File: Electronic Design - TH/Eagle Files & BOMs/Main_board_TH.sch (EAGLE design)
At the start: 41 parts, among them M1 ARDUINO-NANO-3.0, Q1 IRF9520, Q2 IRF9520

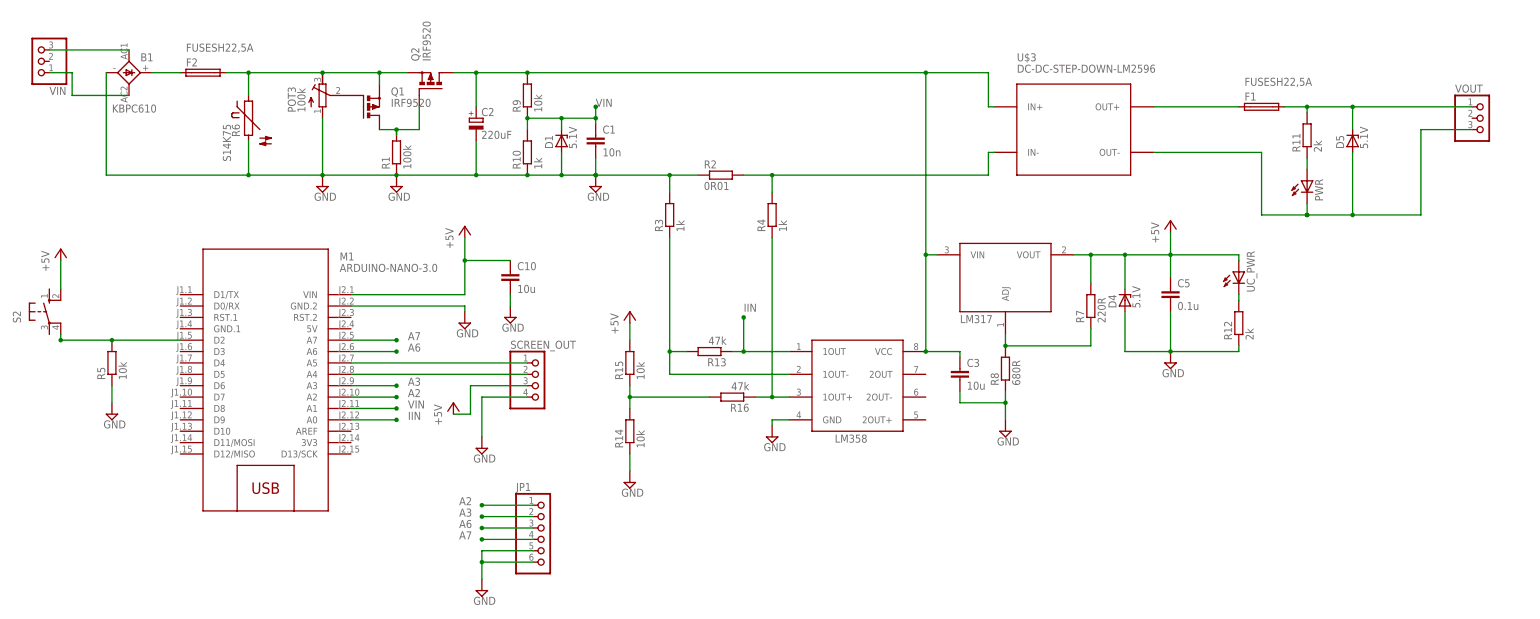
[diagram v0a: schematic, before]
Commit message: Removed: pin headers for arduino, button for arduino and LED for LM2596. Inital board layout complete. Sub modules pretty much done but overall layout still needs work
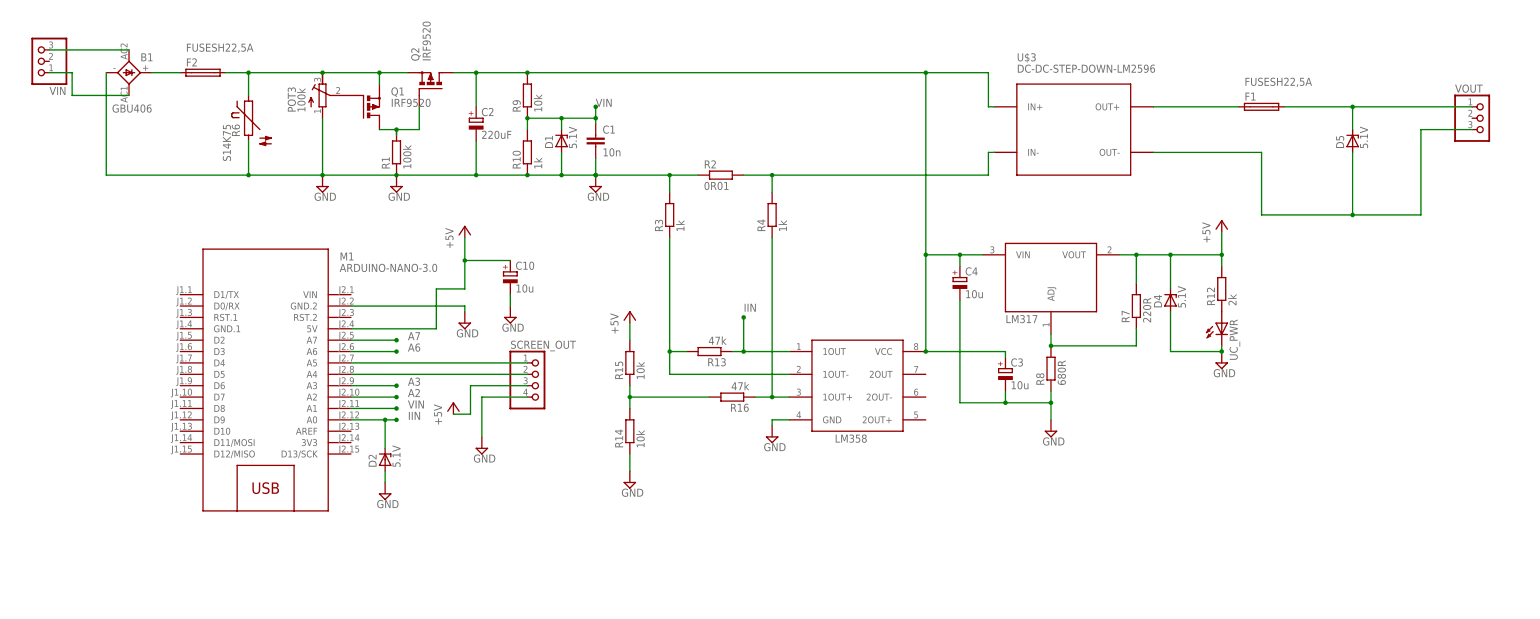
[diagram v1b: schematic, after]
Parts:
- removed C5: 0.1u, resistor:C-EU050-024X044
- removed JP1: (no value), pinhead:PINHD-1X6
- removed PWR: (no value), led:LED3MM
- removed R11: 2k, resistor:R-EU_0207/10
- removed R5: 10k, resistor:R-EU_0207/10
- removed S2: (no value), switch-omron:10-XX
- removed U$1: LM317, Samson:LM317
- added C4: 10u, resistor:CPOL-EUE2.5-7
- added D2: 5.1V, diode:ZPD
- added LM317: LM317, Samson:LM317
- B1: value KBPC610 -> GBU406; device rectifier:GBPC6 -> rectifier:GBU4
- C10, C3: device resistor:C-EU050-024X044 -> resistor:CPOL-EUE2.5-7
- Q1, Q2: device Samson:PMOSFET_PTO220BH -> Samson:PMOSFET_PTO220BV
- renumbered U$2 to LM358
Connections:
- net N$2 renamed A4
- net N$3 renamed A5
- removed net BUTTON: M1.D2, R5.2, S2.P1
- removed net N$18: PWR.A, R11.1
- removed net N$28: R12.2, UC_PWR.C
- new net N$2: R12.1, UC_PWR.A
- net +5V: now also C10.+, LM317.VOUT, M1.5V, R12.2; no longer C10.1, C5.1, M1.VIN, S2.S1, U$1.VOUT, UC_PWR.A
- net A2: no longer JP1.1
- net A3: no longer JP1.2
- net A6: no longer JP1.3
- net A7: no longer JP1.4
- net GND: now also C10.-, C3.-, C4.-, D2.A, UC_PWR.C; no longer C10.2, C3.2, C5.2, JP1.5, JP1.6, R12.1, R5.1
- net IIN: now also D2.C
- net N$10: no longer PWR.C
- net N$23: now also LM317.ADJ; no longer U$1.ADJ
- net VIN_PROTECTED: now also C3.+, C4.+, LM317.VIN; no longer C3.1, U$1.VIN
- net VOUT_FINAL: no longer R11.2
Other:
- moved on the sheet: D4, R12, R7, R8, UC_PWR

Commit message: high level layout complete and adding in BOM
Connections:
- removed net A6: M1.A6
- removed net A7: M1.A7
- removed net IIN: D2.C, LM358.1OUT, M1.A0, R13.1
- removed net VIN: C1.1, D1.C, M1.A1, R10.2, R9.1
- new net A0: D2.C, M1.A0
- new net A1: M1.A1
- new net I_IN: LM358.1OUT, M1.A6, R13.1
- new net V_IN: C1.1, D1.C, M1.A7, R10.2, R9.1
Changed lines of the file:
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@@
 </busses>
 <nets>
-<net name="VIN" class="0">
-<segment>
-<wire x1="-5.08" y1="77.47" x2="-5.08" y2="78.74" width="0.1524" layer="91"/>
-<junction x="-5.08" y="81.28"/>
-<label x="-5.08" y="81.28" size="1.778" layer="95"/>
-<pinref part="C1" gate="G$1" pin="1"/>
-<wire x1="-5.08" y1="78.74" x2="-5.08" y2="81.28" width="0.1524" layer="91"/>
-<wire x1="-12.7" y1="76.2" x2="-12.7" y2="78.74" width="0.1524" layer="91"/>
-<wire x1="-12.7" y1="78.74" x2="-5.08" y2="78.74" width="0.1524" layer="91"/>
-<junction x="-5.08" y="78.74"/>
-<pinref part="D1" gate="G$1" pin="C"/>
-<pinref part="R9" gate="G$1" pin="1"/>
-<wire x1="-12.7" y1="78.74" x2="-20.32" y2="78.74" width="0.1524" layer="91"/>
-<pinref part="R10" gate="G$1" pin="2"/>
-<wire x1="-20.32" y1="78.74" x2="-20.32" y2="76.2" width="0.1524" layer="91"/>
-<junction x="-20.32" y="78.74"/>
-<junction x="-12.7" y="78.74"/>
-</segment>
-<segment>
-<junction x="-49.53" y="13.97"/>
-<label x="-46.99" y="13.97" size="1.778" layer="95"/>
-<wire x1="-49.53" y1="13.97" x2="-59.69" y2="13.97" width="0.1524" layer="91"/>
-<pinref part="M1" gate="G$1" pin="A1"/>
-</segment>
-</net>
-<net name="IIN" class="0">
-<segment>
-<junction x="-49.53" y="11.43"/>
-<label x="-46.99" y="11.43" size="1.778" layer="95"/>
-<wire x1="-59.69" y1="11.43" x2="-52.07" y2="11.43" width="0.1524" layer="91"/>
-<pinref part="M1" gate="G$1" pin="A0"/>
-<pinref part="D2" gate="G$1" pin="C"/>
-<wire x1="-52.07" y1="11.43" x2="-49.53" y2="11.43" width="0.1524" layer="91"/>
-<wire x1="-52.07" y1="11.43" x2="-52.07" y2="5.08" width="0.1524" layer="91"/>
-<junction x="-52.07" y="11.43"/>
-</segment>
-<segment>
-<pinref part="R13" gate="G$1" pin="1"/>
-<pinref part="LM358" gate="G$1" pin="1OUT"/>
-<wire x1="25.4" y1="26.67" x2="27.94" y2="26.67" width="0.1524" layer="91"/>
-<wire x1="29.21" y1="26.67" x2="38.1" y2="26.67" width="0.1524" layer="91"/>
-<wire x1="29.21" y1="26.67" x2="27.94" y2="26.67" width="0.1524" layer="91"/>
-<wire x1="27.94" y1="26.67" x2="27.94" y2="34.29" width="0.1524" layer="91"/>
-<junction x="27.94" y="34.29"/>
-<label x="27.94" y="35.56" size="1.778" layer="95"/>
-<junction x="27.94" y="26.67"/>
-</segment>
-</net>
 <net name="GND" class="0">
 <segment>
@@
 </segment>
 </net>
-<net name="A6" class="0">
-<segment>
-<pinref part="M1" gate="G$1" pin="A6"/>
-<wire x1="-59.69" y1="26.67" x2="-49.53" y2="26.67" width="0.1524" layer="91"/>
-<junction x="-49.53" y="26.67"/>
-<label x="-46.99" y="26.67" size="1.778" layer="95"/>
-</segment>
-</net>
-<net name="A7" class="0">
-<segment>
-<pinref part="M1" gate="G$1" pin="A7"/>
-<wire x1="-59.69" y1="29.21" x2="-49.53" y2="29.21" width="0.1524" layer="91"/>
-<junction x="-49.53" y="29.21"/>
-<label x="-46.99" y="29.21" size="1.778" layer="95"/>
-</segment>
-</net>
 <net name="N$4" class="0">
 <segment>
@@
 </segment>
 </net>
+<net name="V_IN" class="0">
+<segment>
+<wire x1="-5.08" y1="77.47" x2="-5.08" y2="78.74" width="0.1524" layer="91"/>
+<junction x="-5.08" y="81.28"/>
+<label x="-5.08" y="81.28" size="1.778" layer="95"/>
+<pinref part="C1" gate="G$1" pin="1"/>
+<wire x1="-5.08" y1="78.74" x2="-5.08" y2="81.28" width="0.1524" layer="91"/>
+<wire x1="-12.7" y1="76.2" x2="-12.7" y2="78.74" width="0.1524" layer="91"/>
+<wire x1="-12.7" y1="78.74" x2="-5.08" y2="78.74" width="0.1524" layer="91"/>
+<junction x="-5.08" y="78.74"/>
+<pinref part="D1" gate="G$1" pin="C"/>
+<pinref part="R9" gate="G$1" pin="1"/>
+<wire x1="-12.7" y1="78.74" x2="-20.32" y2="78.74" width="0.1524" layer="91"/>
+<pinref part="R10" gate="G$1" pin="2"/>
+<wire x1="-20.32" y1="78.74" x2="-20.32" y2="76.2" width="0.1524" layer="91"/>
+<junction x="-20.32" y="78.74"/>
+<junction x="-12.7" y="78.74"/>
+</segment>
+<segment>
+<pinref part="M1" gate="G$1" pin="A7"/>
+<wire x1="-59.69" y1="29.21" x2="-49.53" y2="29.21" width="0.1524" layer="91"/>
+<junction x="-49.53" y="29.21"/>
+<label x="-46.99" y="29.21" size="1.778" layer="95"/>
+</segment>
+</net>
+<net name="I_IN" class="0">
+<segment>
+<pinref part="R13" gate="G$1" pin="1"/>
+<pinref part="LM358" gate="G$1" pin="1OUT"/>
+<wire x1="25.4" y1="26.67" x2="27.94" y2="26.67" width="0.1524" layer="91"/>
+<wire x1="29.21" y1="26.67" x2="38.1" y2="26.67" width="0.1524" layer="91"/>
+<wire x1="29.21" y1="26.67" x2="27.94" y2="26.67" width="0.1524" layer="91"/>
+<wire x1="27.94" y1="26.67" x2="27.94" y2="34.29" width="0.1524" layer="91"/>
+<junction x="27.94" y="34.29"/>
+<label x="27.94" y="35.56" size="1.778" layer="95"/>
+<junction x="27.94" y="26.67"/>
+</segment>
+<segment>
+<pinref part="M1" gate="G$1" pin="A6"/>
+<wire x1="-59.69" y1="26.67" x2="-49.53" y2="26.67" width="0.1524" layer="91"/>
+<junction x="-49.53" y="26.67"/>
+<label x="-46.99" y="26.67" size="1.778" layer="95"/>
+</segment>
+</net>
+<net name="A1" class="0">
+<segment>
+<junction x="-49.53" y="13.97"/>
+<label x="-46.99" y="13.97" size="1.778" layer="95"/>
+<wire x1="-49.53" y1="13.97" x2="-59.69" y2="13.97" width="0.1524" layer="91"/>
+<pinref part="M1" gate="G$1" pin="A1"/>
+</segment>
+</net>
+<net name="A0" class="0">
+<segment>
+<junction x="-49.53" y="11.43"/>
+<label x="-46.99" y="11.43" size="1.778" layer="95"/>
+<wire x1="-59.69" y1="11.43" x2="-52.07" y2="11.43" width="0.1524" layer="91"/>
+<pinref part="M1" gate="G$1" pin="A0"/>
+<pinref part="D2" gate="G$1" pin="C"/>
+<wire x1="-52.07" y1="11.43" x2="-49.53" y2="11.43" width="0.1524" layer="91"/>
+<wire x1="-52.07" y1="11.43" x2="-52.07" y2="5.08" width="0.1524" layer="91"/>
+<junction x="-52.07" y="11.43"/>
+</segment>
+</net>

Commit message: completing passive protection and active protection alignment and renaming components sequentially (i.e. R1, R2, R3, ...)
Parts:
- removed D5: 5.1V, diode:ZPD
- removed POT3: 100k, resistor:R-TRIMM3296W
- added C5: 10n, resistor:C-EU050-024X044
- added D3: 5.1V, diode:ZPD
- added R11: 1k, resistor:R-EU_0207/10
- added R5: 10k, resistor:R-EU_0207/10
- C1: value 10n -> 220uF; device resistor:C-EU050-024X044 -> resistor:CPOL-EUE3.5-10
- C2: value 220uF -> 10n; device resistor:CPOL-EUE3.5-10 -> resistor:C-EU050-024X044
- R1: value 100k -> S14K75; device resistor:R-EU_0207/10 -> varistor:S14K17
- R10: value 1k -> 0R01; device resistor:R-EU_0207/10 -> resistor:R-EU_0207/15
- R12: value 2k -> 1k
- R14: value 10k -> 47k
- R16: value 47k -> 10k
- R2: value 0R01 -> 10k; device resistor:R-EU_0207/15 -> resistor:R-EU_0207/10
- R3: value 1k -> 10k
- R4: value 1k -> 100k
- R6: value S14K75 -> 1k; device varistor:S14K17 -> resistor:R-EU_0207/10
- R9: value 10k -> 2k
- renumbered C10 to C6, U$3 to LM2596_BUCK_CONVERTER
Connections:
- removed net Q1_GATE: POT3.S, Q1.G
- new net N$3: Q1.G, R2.1, R3.2
- net +5V: now also D2.C, R9.2; no longer D4.C, R12.2
- net A0: no longer D2.C
- net GND: now also C1.-, C2.2, C5.2, D3.A, R1.2, R12.2, R16.1, R3.1, R4.1, R6.1; no longer C1.2, C2.-, D4.A, POT3.A, R1.1, R14.1, R2.1, R3.2, R6.2
- net I_IN: now also C5.1, D3.C
- net N$1: now also F1.1; no longer F2.1
- net N$10: now also D4.A; no longer D5.A
- net N$2: now also R9.1; no longer R12.1
- net N$4: now also R10.2, R11.2; no longer R2.2, R4.2
- net N$5: now also R11.1, R14.1; no longer R16.1, R4.1
- net N$6: now also R12.1; no longer R3.1
- net Q2_GATE: now also R4.2; no longer R1.2
- net VIN_PROTECTED: now also C1.+, R5.2; no longer C2.+, R9.2
- net VIN_UNPROTECTED: now also F1.2, R1.1, R2.2; no longer F2.2, POT3.E, R6.1
- net VOUT_FINAL: now also D4.C, F2.2; no longer D5.C, F1.2
- net VOUT_PREFUSE: now also F2.1; no longer F1.1
- net V_IN: now also C2.1, R5.1, R6.2; no longer C1.1, R10.2, R9.1
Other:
- moved on the sheet: C3, C4, D2, D4, F1, F2, R10, R12, R13, R14, R16, R2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

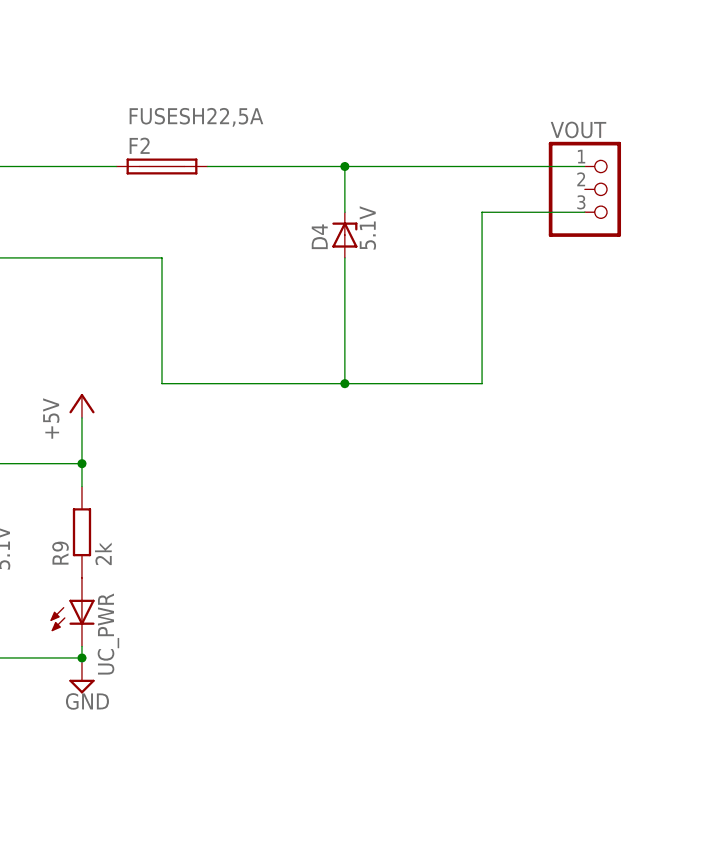
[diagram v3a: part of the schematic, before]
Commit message: adding in USB outputs
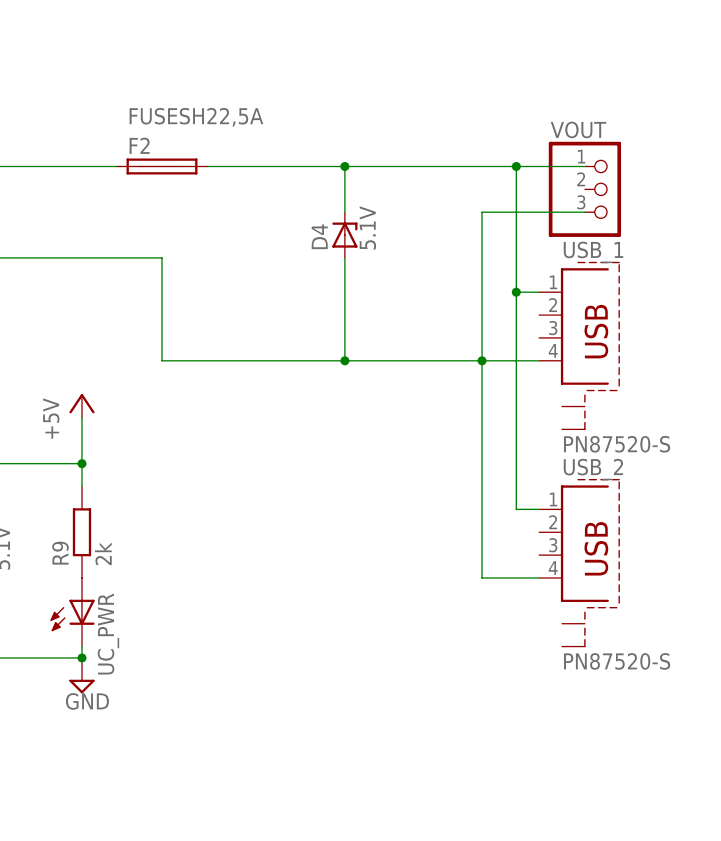
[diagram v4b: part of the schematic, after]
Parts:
- added USB_1, USB_2: PN87520-S, con-berg:PN87520-S
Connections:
- net N$10: now also USB_1.4, USB_2.4
- net VOUT_FINAL: now also USB_1.1, USB_2.1
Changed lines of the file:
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@@
 <part name="R2" library="resistor" deviceset="R-EU_" device="0207/10" value="10k"/>
 <part name="R3" library="resistor" deviceset="R-EU_" device="0207/10" value="10k"/>
+<part name="USB_1" library="con-berg" deviceset="PN87520-S" device=""/>
+<part name="USB_2" library="con-berg" deviceset="PN87520-S" device=""/>
 </parts>
 <sheets>
@@
 <instance part="R2" gate="G$1" x="-68.58" y="83.82" rot="R90"/>
 <instance part="R3" gate="G$1" x="-68.58" y="71.12" rot="R90"/>
+<instance part="USB_1" gate="G$1" x="187.96" y="62.23"/>
+<instance part="USB_2" gate="G$1" x="187.96" y="38.1"/>
 </instances>
 <busses>
@@
 <pinref part="VOUT" gate="A" pin="1"/>
 <wire x1="148.59" y1="81.28" x2="163.83" y2="81.28" width="0.1524" layer="91"/>
-<wire x1="163.83" y1="81.28" x2="190.5" y2="81.28" width="0.1524" layer="91"/>
+<wire x1="163.83" y1="81.28" x2="182.88" y2="81.28" width="0.1524" layer="91"/>
 <junction x="163.83" y="81.28"/>
+<wire x1="182.88" y1="81.28" x2="190.5" y2="81.28" width="0.1524" layer="91"/>
+<wire x1="182.88" y1="81.28" x2="182.88" y2="67.31" width="0.1524" layer="91"/>
+<pinref part="USB_1" gate="G$1" pin="1"/>
+<wire x1="182.88" y1="67.31" x2="185.42" y2="67.31" width="0.1524" layer="91"/>
+<wire x1="182.88" y1="67.31" x2="182.88" y2="43.18" width="0.1524" layer="91"/>
+<pinref part="USB_2" gate="G$1" pin="1"/>
+<wire x1="182.88" y1="43.18" x2="185.42" y2="43.18" width="0.1524" layer="91"/>
+<junction x="182.88" y="67.31"/>
+<junction x="182.88" y="81.28"/>
 </segment>
 </net>
@@
 <pinref part="VOUT" gate="A" pin="3"/>
 <wire x1="190.5" y1="76.2" x2="179.07" y2="76.2" width="0.1524" layer="91"/>
-<wire x1="179.07" y1="76.2" x2="179.07" y2="57.15" width="0.1524" layer="91"/>
-<wire x1="163.83" y1="57.15" x2="179.07" y2="57.15" width="0.1524" layer="91"/>
+<wire x1="179.07" y1="76.2" x2="179.07" y2="59.69" width="0.1524" layer="91"/>
+<wire x1="163.83" y1="59.69" x2="179.07" y2="59.69" width="0.1524" layer="91"/>
 <pinref part="D4" gate="G$1" pin="A"/>
-<wire x1="163.83" y1="71.12" x2="163.83" y2="57.15" width="0.1524" layer="91"/>
-<junction x="163.83" y="57.15"/>
+<wire x1="163.83" y1="71.12" x2="163.83" y2="59.69" width="0.1524" layer="91"/>
+<junction x="163.83" y="59.69"/>
 <pinref part="LM2596_BUCK_CONVERTER" gate="G$1" pin="OUT-"/>
 <wire x1="119.38" y1="71.12" x2="143.51" y2="71.12" width="0.1524" layer="91"/>
-<wire x1="143.51" y1="71.12" x2="143.51" y2="57.15" width="0.1524" layer="91"/>
-<wire x1="143.51" y1="57.15" x2="163.83" y2="57.15" width="0.1524" layer="91"/>
-</segment>
-</net>
+<wire x1="143.51" y1="71.12" x2="143.51" y2="59.69" width="0.1524" layer="91"/>
+<wire x1="143.51" y1="59.69" x2="163.83" y2="59.69" width="0.1524" layer="91"/>
+<pinref part="USB_1" gate="G$1" pin="4"/>
+<wire x1="185.42" y1="59.69" x2="179.07" y2="59.69" width="0.1524" layer="91"/>
+<wire x1="179.07" y1="59.69" x2="179.07" y2="35.56" width="0.1524" layer="91"/>
+<pinref part="USB_2" gate="G$1" pin="4"/>
+<wire x1="179.07" y1="35.56" x2="185.42" y2="35.56" width="0.1524" layer="91"/>
+<junction x="179.07" y="59.69"/>
+</segment>
+</net>
